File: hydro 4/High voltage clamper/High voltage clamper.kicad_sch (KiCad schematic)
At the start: 7 parts, among them Q1 IRF740

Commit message: Updated clamp board
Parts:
- C1: footprint (none) -> Capacitor_THT:CP_Radial_D8.0mm_P2.50mm
- D2: footprint (none) -> Diode_THT:D_DO-15_P12.70mm_Horizontal
- R1, R2: footprint (none) -> Resistor_THT:R_Axial_DIN0207_L6.3mm_D2.5mm_P7.62mm_Horizontal
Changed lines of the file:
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@@
 			)
 		)
-		(property "Footprint" ""
+		(property "Footprint" "Resistor_THT:R_Axial_DIN0207_L6.3mm_D2.5mm_P7.62mm_Horizontal"
 			(at 138.938 82.55 90)
 			(effects
@@
 			)
 		)
-		(property "Footprint" ""
+		(property "Footprint" "Capacitor_THT:CP_Radial_D8.0mm_P2.50mm"
 			(at 121.6152 87.63 0)
 			(effects
@@
 			)
 		)
-		(property "Footprint" ""
+		(property "Footprint" "Diode_THT:D_DO-15_P12.70mm_Horizontal"
 			(at 113.03 73.66 0)
 			(effects
@@
 			)
 		)
-		(property "Footprint" ""
+		(property "Footprint" "Resistor_THT:R_Axial_DIN0207_L6.3mm_D2.5mm_P7.62mm_Horizontal"
 			(at 102.87 75.438 90)
 			(effects

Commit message: Updated schematic
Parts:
- removed C1: 47uF, Capacitor_THT:CP_Radial_D8.0mm_P2.50mm, symbol Device:C_Polarized
- removed D1: ZMDxx, Diode_SMD:D_MiniMELF, symbol Diode:ZMDxx
- removed D2: D, Diode_THT:D_DO-15_P12.70mm_Horizontal, symbol Device:D
- removed LA1: 100Watt 100V, symbol Device:Lamp
- added RV1: 1M, Potentiometer_THT:Potentiometer_ACP_CA14V-15_Vertical_Hole, symbol Device:R_Potentiometer
- R1: value 10k -> 4.7M
- R2: value 100k -> 50 200watt; footprint Resistor_THT:R_Axial_DIN0207_L6.3mm_D2.5mm_P7.62mm_Horizontal -> Resistor_THT:R_Box_L26.0mm_W5.0mm_P20.00mm
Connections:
- net +VDC: now also R1.2, R2.2; no longer R1.1
- net -VDC: now also RV1.3; no longer R2.1
- net at Q1.1 (G): now also RV1.2; no longer R2.2
- net at Q1.2 (D): now also R2.1
- new net: R1.1, RV1.1
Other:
- note added: "Setup pot for startb conducting at 52V.. full at about 64V.."
- moved on the sheet: R1

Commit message: Updated schematic
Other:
- company: (none) -> Yr-design
- title: (none) -> Hight voltage clamping for Hydro V4
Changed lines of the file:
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@@
 	(paper "A4")
 	(title_block
+		(title "Hight voltage clamping for Hydro V4")
 		(date "2023-12-25")
+		(rev "V0.9")
+		(company "Yr-design")
+		(comment 1 "Clamps top voltage slowly to apply the load resistors")
 	)
 	(junction

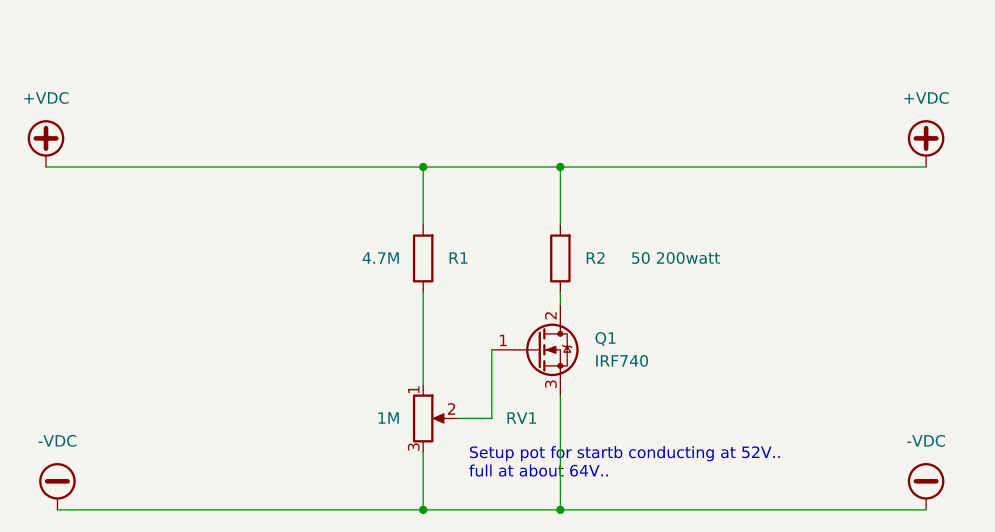
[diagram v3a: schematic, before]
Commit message: Changed to fixed resistors
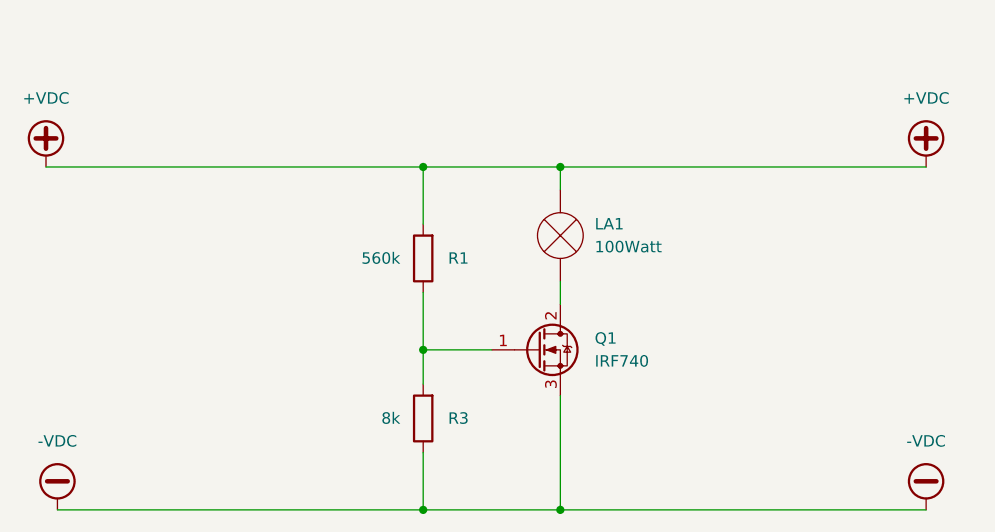
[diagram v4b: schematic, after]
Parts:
- removed R2: 50 200watt, Resistor_THT:R_Box_L26.0mm_W5.0mm_P20.00mm, symbol Device:R
- removed RV1: 1M, Potentiometer_THT:Potentiometer_ACP_CA14V-15_Vertical_Hole, symbol Device:R_Potentiometer
- added LA1: 100Watt, symbol Device:Lamp
- added R3: 8k, Resistor_THT:R_Axial_DIN0207_L6.3mm_D2.5mm_P7.62mm_Horizontal, symbol Device:R
- R1: value 4.7M -> 560k
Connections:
- net +VDC: now also LA1.2 (+)
- net -VDC: now also R3.1
- net at Q1.2 (D): now also LA1.1 (-)
- net at Q1.1 (G): now also R1.1, R3.2
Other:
- note removed: "Setup pot for startb conducting at 52V.. full at about 64V.."
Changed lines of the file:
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@@
+	)
+	(junction
+		(at 147.32 91.44)
+		(diameter 0)
+		(color 0 0 0 0)
+	)
+	(junction
+		(at 132.08 73.66)
+		(diameter 0)
+		(color 0 0 0 0)
 	)
 	(junction
@@
 	)
 	(junction
-		(at 147.32 91.44)
-		(diameter 0)
-		(color 0 0 0 0)
-	)
-	(junction
 		(at 132.08 53.34)
 		(diameter 0)
@@
 	(wire
 		(pts
-			(xy 139.7 81.28) (xy 139.7 73.66)
-		)
-		(stroke
-			(width 0)
-			(type default)
-		)
-	)
-	(wire
-		(pts
-			(xy 132.08 67.31) (xy 132.08 77.47)
-		)
-		(stroke
-			(width 0)
-			(type default)
-		)
-	)
-	(wire
-		(pts
-			(xy 135.89 81.28) (xy 139.7 81.28)
+			(xy 132.08 73.66) (xy 132.08 77.47)
+		)
+		(stroke
+			(width 0)
+			(type default)
+		)
+	)
+	(wire
+		(pts
+			(xy 132.08 67.31) (xy 132.08 73.66)
+		)
+		(stroke
+			(width 0)
+			(type default)
+		)
+	)
+	(wire
+		(pts
+			(xy 147.32 53.34) (xy 147.32 55.88)
+		)
+		(stroke
+			(width 0)
+			(type default)
+		)
+	)
+	(wire
+		(pts
+			(xy 132.08 73.66) (xy 139.7 73.66)
 		)
 		(stroke
@@
 	(wire
 		(pts
+			(xy 147.32 53.34) (xy 187.96 53.34)
+		)
+		(stroke
+			(width 0)
+			(type default)
+		)
+	)
+	(wire
+		(pts
 			(xy 91.44 91.44) (xy 132.08 91.44)
 		)
@@
 	(wire
 		(pts
-			(xy 147.32 53.34) (xy 187.96 53.34)
+			(xy 147.32 66.04) (xy 147.32 68.58)
 		)
 		(stroke
@@
 		)
 	)
-	(wire
-		(pts
-			(xy 147.32 53.34) (xy 147.32 59.69)
-		)
-		(stroke
-			(width 0)
-			(type default)
-		)
-	)
-	(wire
-		(pts
-			(xy 147.32 67.31) (xy 147.32 68.58)
-		)
-		(stroke
-			(width 0)
-			(type default)
-		)
-	)
-	(text "Setup pot for startb conducting at 52V.. \nfull at about 64V.."
-		(exclude_from_sim no)
-		(at 137.16 86.36 0)
-		(effects
-			(font
-				(size 1.27 1.27)
-			)
-			(justify left)
-		)
-	)
 	(symbol
 		(lib_id "Device:R")
-		(at 147.32 63.5 180)
-		(unit 1)
-		(exclude_from_sim no)
-		(in_bom yes)
-		(on_board yes)
-		(dnp no)
-		(property "Reference" "R2"
-			(at 152.4 63.5 0)
-			(effects
-				(font
-					(size 1.27 1.27)
-				)
-				(justify left)
-			)
-		)
-		(property "Value" "50 200watt"
-			(at 165.1 63.5 0)
-			(effects
-				(font
-					(size 1.27 1.27)
-				)
-				(justify left)
-			)
-		)
-		(property "Footprint" "Resistor_THT:R_Box_L26.0mm_W5.0mm_P20.00mm"
-			(at 149.098 63.5 90)
+		(at 132.08 81.28 180)
+		(unit 1)
+		(exclude_from_sim no)
+		(in_bom yes)
+		(on_board yes)
+		(dnp no)
+		(property "Reference" "R3"
+			(at 137.16 81.28 0)
+			(effects
+				(font
+					(size 1.27 1.27)
+				)
+				(justify left)
+			)
+		)
+		(property "Value" "8k"
+			(at 129.54 81.28 0)
+			(effects
+				(font
+					(size 1.27 1.27)
+				)
+				(justify left)
+			)
+		)
+		(property "Footprint" "Resistor_THT:R_Axial_DIN0207_L6.3mm_D2.5mm_P7.62mm_Horizontal"
+			(at 133.858 81.28 90)
 			(effects
 				(font
@@
 		)
 		(property "Datasheet" "~"
-			(at 147.32 63.5 0)
+			(at 132.08 81.28 0)
 			(effects
 				(font
@@
 		)
 		(property "Description" "Resistor"
-			(at 147.32 63.5 0)
+			(at 132.08 81.28 0)
 			(effects
 				(font
@@
 			(project "High voltage clamper"
 				(path "/0c579c7f-c211-4bd8-99a0-966a9097b02e"
-					(reference "R2")
+					(reference "R3")
 					(unit 1)
 				)
@@
 	)
 	(symbol
+		(lib_id "Device:Lamp")
+		(at 147.32 60.96 0)
+		(unit 1)
+		(exclude_from_sim no)
+		(in_bom yes)
+		(on_board yes)
+		(dnp no)
+		(fields_autoplaced yes)
+		(property "Reference" "LA1"
+			(at 151.13 59.6899 0)
+			(effects
+				(font
+					(size 1.27 1.27)
+				)
+				(justify left)
+			)
+		)
+		(property "Value" "100Watt"
+			(at 151.13 62.2299 0)
+			(effects
+				(font
+					(size 1.27 1.27)
+				)
+				(justify left)
+			)
+		)
+		(property "Footprint" ""
+			(at 147.32 58.42 90)
+			(effects
+				(font
+					(size 1.27 1.27)
+				)
+				(hide yes)
+			)
+		)
+		(property "Datasheet" "~"
+			(at 147.32 58.42 90)
+			(effects
+				(font
+					(size 1.27 1.27)
+				)
+				(hide yes)
+			)
+		)
+		(property "Description" "Lamp"
+			(at 147.32 60.96 0)
+			(effects
+				(font
+					(size 1.27 1.27)
+				)
+				(hide yes)
+			)
+		)
+		(pin "1"
+		)
+		(pin "2"
+		)
+		(instances
+			(project "High voltage clamper"
+				(path "/0c579c7f-c211-4bd8-99a0-966a9097b02e"
+					(reference "LA1")
+					(unit 1)
+				)
+			)
+		)
+	)
+	(symbol
 		(lib_id "Device:R")
 		(at 132.08 63.5 180)
@@
 			)
 		)
-		(property "Value" "4.7M"
+		(property "Value" "560k"
 			(at 129.54 63.5 0)
 			(effects
@@
 					(unit 1)
 				)
-			)
-		)
-	)
-	(symbol
-		(lib_id "Device:R_Potentiometer")
-		(at 132.08 81.28 0)
-		(unit 1)
-		(exclude_from_sim no)
-		(in_bom yes)
-		(on_board yes)
-		(dnp no)
-		(property "Reference" "RV1"
-			(at 144.78 81.28 0)
-			(effects
-				(font
-					(size 1.27 1.27)
-				)
-				(justify right)
-			)
-		)
-		(property "Value" "1M"
-			(at 129.54 81.28 0)
-			(effects
-				(font
-					(size 1.27 1.27)
-				)
-				(justify right)
-			)
-		)
-		(property "Footprint" "Potentiometer_THT:Potentiometer_ACP_CA14V-15_Vertical_Hole"
-			(at 132.08 81.28 0)
-			(effects
-				(font
-					(size 1.27 1.27)
-				)
-				(hide yes)
-			)
-		)
-		(property "Datasheet" "~"
-			(at 132.08 81.28 0)
-			(effects
-				(font
-					(size 1.27 1.27)
-				)
-				(hide yes)
-			)
-		)
-		(property "Description" "Potentiometer"
-			(at 132.08 81.28 0)
-			(effects
-				(font
-					(size 1.27 1.27)
-				)
-				(hide yes)
-			)
-		)
-		(pin "2"
-		)
-		(pin "3"
-		)
-		(pin "1"
-		)
-		(instances
-			(project "High voltage clamper"
-				(path "/0c579c7f-c211-4bd8-99a0-966a9097b02e"
-					(reference "RV1")
-					(unit 1)
-				)
